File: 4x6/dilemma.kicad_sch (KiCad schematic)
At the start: 328 parts, among them J1 USB_C_Receptacle_USB2.0, J102 NA_serial, J105 NA_Conn_01x04_Female, J113 Cirque, J3 NA_GC9A01, J4 Conn_01x05, J5 NA_Conn_01x02, J5001 USB_C_Receptacle_USB2.0, J5002 NA_Conn_01x02, J5003 NA_serial, J5004 NA_GC9A01, J5005 NA_Conn_01x04_Female, J5007 Cirque, J5008 Conn_01x05, J5009 Conn_01x05, J5010 Conn_01x05, SW1 SW_Push, SW101 NA_SW_Push, SW102 NA_SW_Push, SW103 NA_SW_Push, SW104 NA_SW_Push, SW105 NA_SW_Push, SW106 NA_SW_Push, SW107 NA_SW_Push, SW108 NA_SW_Push, SW109 NA_SW_Push, SW112 NA_SW_Push, SW113 NA_SW_Push, SW114 NA_SW_Push, SW115 NA_SW_Push, SW116 NA_SW_Push, SW117 NA_SW_Push, SW118 NA_SW_Push, SW119 NA_SW_Push, SW3001 NA_SW_Push, SW3002 NA_RotaryEncoder_Switch, SW5001 SW_Push, SW5002 NA_SW_Push, SW5003 NA_SW_Push, SW5004 NA_SW_Push, SW5005 NA_SW_Push, SW5006 NA_SW_Push, SW5007 NA_SW_Push, SW5008 NA_SW_Push, SW5009 NA_SW_Push, SW5010 NA_SW_Push, SW5011 NA_SW_Push, SW5012 NA_SW_Push, SW5013 NA_SW_Push, SW5014 NA_SW_Push, SW5015 NA_SW_Push, SW5016 NA_SW_Push, SW5017 NA_SW_Push, SW5018 NA_SW_Push, SW5019 NA_SW_Push, SW5020 NA_RotaryEncoder_Switch, SW5021 SW_SPST, SW5022 SW_SPST, SW5023 NA_SW_Push, SW5024 NA_SW_Push, SW5025 NA_SW_Push, SW5026 NA_SW_Push, SW5027 NA_SW_Push, SW5028 NA_SW_Push, SW5029 NA_SW_Push, SW5030 NA_SW_Push, SW5031 NA_SW_Push, SW5032 NA_SW_Push, SW5033 NA_SW_Push, SW5034 NA_SW_Push, SW5035 NA_SW_Push, SW5036 NA_SW_Push, SW5037 NA_SW_Push, SW5038 NA_SW_Push, SW5039 NA_SW_Push, SW5040 NA_SW_Push, U1 RP2040, U2 W25Q128JVS, U3 XC6210B332MR-G, U4 USBLC6-2P6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

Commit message: switches, routing
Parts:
- added D5015, D5126: D_matrix, local-libraries:D_0402, symbol Device:D
- added SW5041, SW5042: NA_SW_Push, local-libraries:SW_MX_choc, symbol Switch:SW_Push
- added U5005, U5006: USBLC6-2P6, local-libraries:SOT-666, symbol Power_Protection:USBLC6-2P6
- U4, U5003: footprint Package_TO_SOT_SMD:SOT-666 -> local-libraries:SOT-666
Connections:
- net +3V3: now also U5005.5 (VBUS)
- net +3V3_L: now also U5006.5 (VBUS)
- net GND: now also U5005.2 (GND)
- net GND_L: now also U5006.2 (GND)
- net M_COL4: now also D5015.1 (K)
- net M_COL4_L: now also D5126.1 (K)
- net M_ROW1: now also SW5041.1
- net M_ROW1_L: now also SW5042.1
- net SERIAL: now also U5005.1 (I/O1), U5005.6 (I/O1)
- net SERIAL_L: now also U5006.1 (I/O1), U5006.6 (I/O1)
- new net: D5015.2 (A), SW5041.2
- new net: D5126.2 (A), SW5042.2
- no-connect marks 23 -> 27

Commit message: routing
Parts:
- added D5127, D5137: SK6812MINI, local-libraries:SK6812_mini_e_corners, symbol LED:SK6812MINI
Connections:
- net +3V3: now also D5127.4 (VDD)
- net +3V3_L: now also D5137.4 (VDD)
- net GND: now also D5127.2 (VSS)
- net GND_L: now also D5137.2 (VSS)
- net at D5033.1 (DOUT): now also D5127.3 (DIN)
- net at D5051.1 (DOUT): now also D5137.3 (DIN)
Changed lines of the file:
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@@
   (junction (at 123.19 232.41) (diameter 0) (color 0 0 0 0)
   )
-  (no_connect (at 833.755 222.25))
   (no_connect (at 342.265 50.8))
   (no_connect (at 342.265 40.64))
@@
   (no_connect (at 332.74 180.34))
   (no_connect (at 339.725 335.915))
+  (no_connect (at 854.075 159.385))
   (no_connect (at 48.26 360.045))
   (no_connect (at 339.725 338.455))
   (no_connect (at 657.86 307.34))
   (no_connect (at 322.58 481.33))
+  (no_connect (at 859.155 222.25))
   (no_connect (at 271.78 176.53))
   (no_connect (at 264.16 473.71))
@@
   (no_connect (at 339.725 356.235))
   (no_connect (at 339.725 358.775))
-  (no_connect (at 828.675 159.385))
   (no_connect (at 48.26 362.585))
   (polyline (pts (xy 348.615 167.005) (xy 348.615 191.77))
@@
     (stroke (width 0) (type default))
   )
+  (wire (pts (xy 828.675 159.385) (xy 838.835 159.385))
+    (stroke (width 0) (type default))
+  )
   (wire (pts (xy 358.775 423.545) (xy 365.125 423.545))
     (stroke (width 0) (type default))
@@
     (stroke (width 0) (type default))
   )
+  (wire (pts (xy 833.755 222.25) (xy 843.915 222.25))
+    (stroke (width 0) (type default))
+  )
   (wire (pts (xy 143.51 36.83) (xy 143.51 38.1))
     (stroke (width 0) (type default))
@@
     (fill (type none))
   )
-  (rectangle (start 818.515 237.49) (end 843.915 262.89)
+  (rectangle (start 838.835 209.55) (end 864.235 234.95)
     (stroke (width 0.2) (type dot))
     (fill (type none))
@@
     (fill (type none))
   )
-  (rectangle (start 815.975 121.285) (end 841.375 146.685)
+  (rectangle (start 833.755 146.685) (end 859.155 172.085)
     (stroke (width 0.2) (type dot))
     (fill (type none))
@@
     )
   )
+  (symbol (lib_id "power_L:GND_L") (at 851.535 229.87 0) (unit 1)
+    (in_bom yes) (on_board yes) (dnp no)
+    (property "Reference" "#PWR05184" (at 851.535 236.22 0)
+      (effects (font (size 1.27 1.27)) hide)
+    )
+    (property "Value" "GND_L" (at 856.615 232.41 0)
+      (effects (font (size 1.27 1.27)))
+    )
+    (property "Footprint" "" (at 851.535 229.87 0)
+      (effects (font (size 1.27 1.27)) hide)
+    )
+    (property "Datasheet" "" (at 851.535 229.87 0)
+      (effects (font (size 1.27 1.27)) hide)
+    )
+    (pin "1")
+    (instances
+      (project "dilemma"
+        (path "/7353e96a-343a-4876-b497-b1d205a14d97"
+          (reference "#PWR05184") (unit 1)
+        )
+      )
+    )
+  )
   (symbol (lib_id "LED:SK6812MINI") (at 739.775 70.485 0) (unit 1)
     (in_bom yes) (on_board yes) (dnp no)
@@
     )
   )
+  (symbol (lib_id "LED:SK6812MINI") (at 846.455 159.385 0) (unit 1)
+    (in_bom yes) (on_board yes) (dnp no)
+    (property "Reference" "D5127" (at 847.725 153.035 0)
+      (effects (font (size 1.27 1.27)))
+    )
+    (property "Value" "SK6812MINI" (at 852.805 165.735 0)
+      (effects (font (size 1.27 1.27)))
+    )
+    (property "Footprint" "local-libraries:SK6812_mini_e_corners" (at 847.725 167.005 0)
+      (effects (font (size 1.27 1.27)) (justify left top) hide)
+    )
+    (property "Datasheet" "https://cdn-shop.adafruit.com/product-files/2686/SK6812MINI_REV.01-1-2.pdf" (at 848.995 168.91 0)
+      (effects (font (size 1.27 1.27)) (justify left top) hide)
+    )
+    (pin "1")
+    (pin "2")
+    (pin "3")
+    (pin "4")
+    (instances
+      (project "dilemma"
+        (path "/7353e96a-343a-4876-b497-b1d205a14d97"
+          (reference "D5127") (unit 1)
+        )
+      )
+    )
+  )
   (symbol (lib_id "Device:C") (at 128.27 475.615 0) (unit 1)
     (in_bom yes) (on_board yes) (dnp no)
@@
     )
   )
+  (symbol (lib_id "power_L:+3V3_L") (at 851.535 214.63 0) (unit 1)
+    (in_bom yes) (on_board yes) (dnp no)
+    (property "Reference" "#PWR05183" (at 851.535 218.44 0)
+      (effects (font (size 1.27 1.27)) hide)
+    )
+    (property "Value" "+3V3_L" (at 856.615 212.09 0)
+      (effects (font (size 1.27 1.27)))
+    )
+    (property "Footprint" "" (at 851.535 214.63 0)
+      (effects (font (size 1.27 1.27)) hide)
+    )
+    (property "Datasheet" "" (at 851.535 214.63 0)
+      (effects (font (size 1.27 1.27)) hide)
+    )
+    (pin "1")
+    (instances
+      (project "dilemma"
+        (path "/7353e96a-343a-4876-b497-b1d205a14d97"
+          (reference "#PWR05183") (unit 1)
+        )
+      )
+    )
+  )
   (symbol (lib_id "Mechanical:MountingHole_Pad") (at 184.15 176.53 0) (unit 1)
     (in_bom yes) (on_board yes) (dnp no)
@@
     )
   )
+  (symbol (lib_id "power:GND") (at 846.455 167.005 0) (unit 1)
+    (in_bom yes) (on_board yes) (dnp no)
+    (property "Reference" "#PWR05182" (at 846.455 173.355 0)
+      (effects (font (size 1.27 1.27)) hide)
+    )
+    (property "Value" "GND" (at 846.455 170.815 0)
+      (effects (font (size 1.27 1.27)))
+    )
+    (property "Footprint" "" (at 846.455 167.005 0)
+      (effects (font (size 1.27 1.27)) hide)
+    )
+    (property "Datasheet" "" (at 846.455 167.005 0)
+      (effects (font (size 1.27 1.27)) hide)
+    )
+    (pin "1")
+    (instances
+      (project "dilemma"
+        (path "/7353e96a-343a-4876-b497-b1d205a14d97"
+          (reference "#PWR05182") (unit 1)
+        )
+      )
+    )
+  )
   (symbol (lib_id "power_L:+3V3_L") (at 790.575 245.11 0) (unit 1)
     (in_bom yes) (on_board yes) (dnp no)
@@
     )
   )
+  (symbol (lib_id "power:+3.3V") (at 846.455 151.765 0) (unit 1)
+    (in_bom yes) (on_board yes) (dnp no)
+    (property "Reference" "#PWR05181" (at 846.455 155.575 0)
+      (effects (font (size 1.27 1.27)) hide)
+    )
+    (property "Value" "+3.3V" (at 847.725 147.955 0)
+      (effects (font (size 1.27 1.27)))
+    )
+    (property "Footprint" "" (at 846.455 151.765 0)
+      (effects (font (size 1.27 1.27)) hide)
+    )
+    (property "Datasheet" "" (at 846.455 151.765 0)
+      (effects (font (size 1.27 1.27)) hide)
+    )
+    (pin "1")
+    (instances
+      (project "dilemma"
+        (path "/7353e96a-343a-4876-b497-b1d205a14d97"
+          (reference "#PWR05181") (unit 1)
+        )
+      )
+    )
+  )
   (symbol (lib_id "sk6805-ec15:SK6805-EC15") (at 509.27 351.79 0) (unit 1)
     (in_bom yes) (on_board yes) (dnp no)
@@
         )
       )
+    )
+  )
+  (symbol (lib_id "LED:SK6812MINI") (at 851.535 222.25 0) (unit 1)
+    (in_bom yes) (on_board yes) (dnp no)
+    (property "Reference" "D5137" (at 852.805 215.9 0)
+      (effects (font (size 1.27 1.27)))
+    )
+    (property "Value" "SK6812MINI" (at 857.885 228.6 0)
+      (effects (font (size 1.27 1.27)))
+    )
+    (property "Footprint" "local-libraries:SK6812_mini_e_corners" (at 852.805 229.87 0)
+      (effects (font (size 1.27 1.27)) (justify left top) hide)
+    )
+    (property "Datasheet" "https://cdn-shop.adafruit.com/product-files/2686/SK6812MINI_REV.01-1-2.pdf" (at 854.075 231.775 0)
+      (effects (font (size 1.27 1.27)) (justify left top) hide)
+    )
+    (pin "1")
+    (pin "2")
+    (pin "3")
+    (pin "4")
+    (instances
+      (project "dilemma"
+        (path "/7353e96a-343a-4876-b497-b1d205a14d97"
+          (reference "D5137") (unit 1)
+        )
+      )

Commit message: silkscreen
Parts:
- added D5138, D5139, D5140, D5141, D5142, D5143: SK6805-EC15, local-libraries:LED_SK6805-EC15_1.5x1.5mm_P0.6mm_handsolder, symbol sk6805-ec15:SK6805-EC15
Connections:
- net +3V3: now also D5138.2 (VDD), D5139.2 (VDD), D5140.2 (VDD)
- net +3V3_L: now also D5141.2 (VDD), D5142.2 (VDD), D5143.2 (VDD)
- net GND: now also D5138.4 (GND), D5139.4 (GND), D5140.4 (GND)
- net GND_L: now also D5141.4 (GND), D5142.4 (GND), D5143.4 (GND)
- net at D5029.1 (DIN): now also D5143.3 (DOUT); no longer D5027.3 (DOUT)
- net at D22.3 (DOUT): now also D5138.1 (DIN); no longer D25.1 (DIN)
- new net: D5027.3 (DOUT), D5141.1 (DIN)
- new net: D5141.3 (DOUT), D5142.1 (DIN)
- new net: D5142.3 (DOUT), D5143.1 (DIN)
- new net: D5138.3 (DOUT), D5139.1 (DIN)
- new net: D5139.3 (DOUT), D5140.1 (DIN)
- new net: D25.1 (DIN), D5140.3 (DOUT)
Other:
- moved on the sheet: C5017, C5018, D25, D28, D5029, D5030, D5031, D5032, D5033, D5034, D5035, D5036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

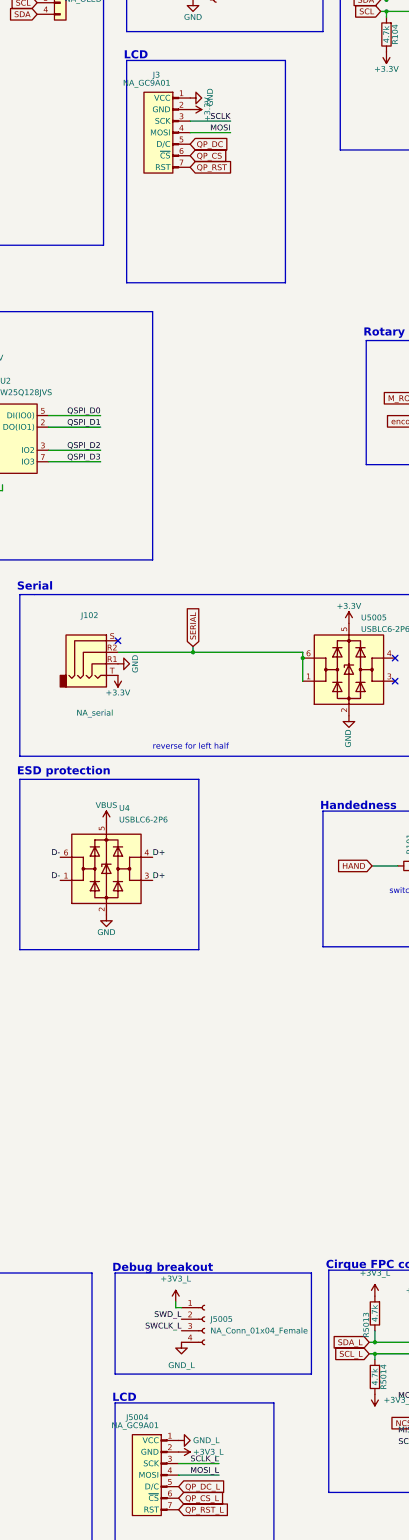
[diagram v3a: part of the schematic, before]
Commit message: fix lcd pinout
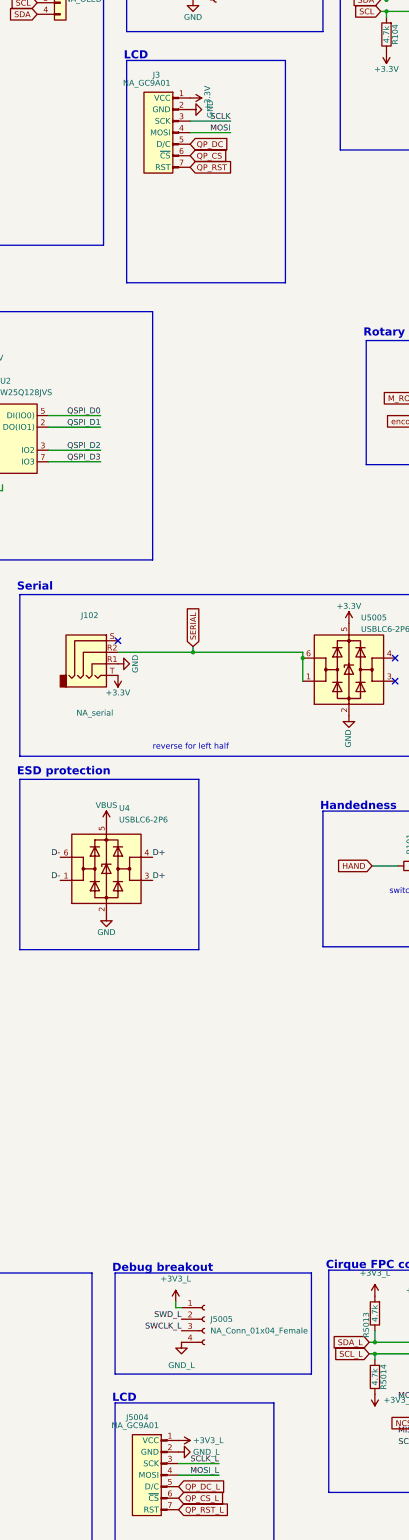
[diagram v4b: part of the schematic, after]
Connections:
- net +3V3: now also J3.1 (VCC); no longer J3.2 (GND)
- net +3V3_L: now also J5004.1 (VCC); no longer J5004.2 (GND)
- net GND: now also J3.2 (GND); no longer J3.1 (VCC)
- net GND_L: now also J5004.2 (GND); no longer J5004.1 (VCC)
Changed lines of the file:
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@@
     )
   )
-  (symbol (lib_id "power_L:+3V3_L") (at 285.115 354.965 270) (unit 1)
+  (symbol (lib_id "power_L:+3V3_L") (at 285.115 352.425 270) (unit 1)
     (in_bom yes) (on_board yes) (dnp no) (fields_autoplaced)
-    (property "Reference" "#PWR05043" (at 281.305 354.965 0)
+    (property "Reference" "#PWR05043" (at 281.305 352.425 0)
       (effects (font (size 1.27 1.27)) hide)
     )
-    (property "Value" "+3V3_L" (at 288.29 354.9649 90)
+    (property "Value" "+3V3_L" (at 288.29 352.4249 90)
       (effects (font (size 1.27 1.27)) (justify left))
     )
-    (property "Footprint" "" (at 285.115 354.965 0)
+    (property "Footprint" "" (at 285.115 352.425 0)
       (effects (font (size 1.27 1.27)) hide)
     )
-    (property "Datasheet" "" (at 285.115 354.965 0)
+    (property "Datasheet" "" (at 285.115 352.425 0)
       (effects (font (size 1.27 1.27)) hide)
     )
@@
     )
   )
-  (symbol (lib_id "power:+3.3V") (at 287.655 59.69 270) (unit 1)
+  (symbol (lib_id "power:+3.3V") (at 287.655 57.15 270) (unit 1)
     (in_bom yes) (on_board yes) (dnp no)
-    (property "Reference" "#PWR0109" (at 283.845 59.69 0)
+    (property "Reference" "#PWR0109" (at 283.845 57.15 0)
       (effects (font (size 1.27 1.27)) hide)
     )
-    (property "Value" "+3.3V" (at 291.465 59.69 0)
+    (property "Value" "+3.3V" (at 291.465 57.15 0)
       (effects (font (size 1.27 1.27)))
     )
-    (property "Footprint" "" (at 287.655 59.69 0)
+    (property "Footprint" "" (at 287.655 57.15 0)
       (effects (font (size 1.27 1.27)) hide)
     )
-    (property "Datasheet" "" (at 287.655 59.69 0)
+    (property "Datasheet" "" (at 287.655 57.15 0)
       (effects (font (size 1.27 1.27)) hide)
     )
@@
     )
   )
-  (symbol (lib_id "power_L:GND_L") (at 285.115 352.425 90) (unit 1)
+  (symbol (lib_id "power_L:GND_L") (at 285.115 354.965 90) (unit 1)
     (in_bom yes) (on_board yes) (dnp no) (fields_autoplaced)
-    (property "Reference" "#PWR05044" (at 291.465 352.425 0)
+    (property "Reference" "#PWR05044" (at 291.465 354.965 0)
       (effects (font (size 1.27 1.27)) hide)
     )
-    (property "Value" "GND_L" (at 288.29 352.4249 90)
+    (property "Value" "GND_L" (at 288.29 354.9649 90)
       (effects (font (size 1.27 1.27)) (justify right))
     )
-    (property "Footprint" "" (at 285.115 352.425 0)
+    (property "Footprint" "" (at 285.115 354.965 0)
       (effects (font (size 1.27 1.27)) hide)
     )
-    (property "Datasheet" "" (at 285.115 352.425 0)
+    (property "Datasheet" "" (at 285.115 354.965 0)
       (effects (font (size 1.27 1.27)) hide)
     )
@@
     )
   )
-  (symbol (lib_id "power:GND") (at 287.655 57.15 90) (unit 1)
+  (symbol (lib_id "power:GND") (at 287.655 59.69 90) (unit 1)
     (in_bom yes) (on_board yes) (dnp no)
-    (property "Reference" "#PWR0106" (at 294.005 57.15 0)
+    (property "Reference" "#PWR0106" (at 294.005 59.69 0)
       (effects (font (size 1.27 1.27)) hide)
     )
-    (property "Value" "GND" (at 292.0492 57.023 0)
+    (property "Value" "GND" (at 292.0492 59.563 0)
       (effects (font (size 1.27 1.27)))
     )
-    (property "Footprint" "" (at 287.655 57.15 0)
+    (property "Footprint" "" (at 287.655 59.69 0)
       (effects (font (size 1.27 1.27)) hide)
     )
-    (property "Datasheet" "" (at 287.655 57.15 0)
+    (property "Datasheet" "" (at 287.655 59.69 0)
       (effects (font (size 1.27 1.27)) hide)
     )
